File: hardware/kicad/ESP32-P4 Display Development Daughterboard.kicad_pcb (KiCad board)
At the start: 2 copper layers, 130 x 100 mm, 199 parts, among them J1001 SSQ-113-01-G-D, J1002 SSQ-113-01-G-D, J1003 DEBUG HEADER, J201 VEHICLE 12V, J501 SERVICE LINK 5V, J701 NANO DSI 15P, J702 DISPLAYMAN LCD 40P, J801 GT9271 TOUCH 8P, J901 BL HARD DISABLE, Q201 CSD19531Q5A, Q202 CSD19531Q5A, Q301 CSD19531Q5A, Q302 CSD19531Q5A, Q303 CSD19531Q5A, Q304 CSD19531Q5A, Q801 MMBT3904, U201 LM74800QDRRRQ1, U301 LM5176QPWPRQ1, U501 LM76003RNPR, U502 TPS259470ARPWR, U601 TPS3808G01DBVR, U602 LM3880MF-1AA/NOPB, U603 TLV75518PDBVR, U604 TLV75528PDBVR, U605 TPS22919DCKR, U606 SN74LVC1G07DBVR, U607 SN74LVC1G07DBVR, U608 SN74LVC1G07DBVR, U701 TPD6E05U06RVZR, U801 TLV75533PDBVR, U802 TMUX1574PWR, U803 TPD4E05U06DQAR, U901 TPS922053DYYR, U902 SN74LVC1G11DCKR

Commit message: Major fixes. Needs simplification, component organization and routing
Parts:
- J201: footprint Phase2:Molex_Micro-Fit_3.0_43045-0218_2x01-1MP_P3.00mm_Vertical -> Phase2:CONN_SD-43045-007_02_MOL
- J701: footprint Phase2:Amphenol_SFW15R-2STE1LF -> Phase2:Amphenol_CON15_1X15_DRB_SFW_FCI
- J702: footprint Phase2:Molex_505110-4096 -> Phase2:Molex_CON_5051104096
- J801: value GT9271 TOUCH 8P -> Wurth 8pin Top Contact FPC; footprint Connector_FFC-FPC:Hirose_FH12-8S-0.5SH_1x08-1MP_P0.50mm_Horizontal -> Phase2:Wurth_68710814022
- Q201, Q202, Q301, Q302, Q303, Q304: footprint Package_SON:Texas_DQK -> Phase2:Texas_DQJ0008A_VSONP-8
- U502: footprint Phase2:Texas_RPW0010A_VQFN-HR-10_2x2mm -> Phase2:RPW0010A-MFG
- moved TP504 279.8 mm to (-120.5, -63.0)
- moved TP501 272.7 mm to (-103.0, -63.0)
- moved TP503 263.3 mm to (-108.5, -63.0)
- moved R512 252.3 mm to (-106.9, -34.0), turned to 180 degrees
- moved R510 251.8 mm to (-88.5, -48.5)
- moved C513 251.1 mm to (-118.2, -35.0), turned to 180 degrees
- moved R505 249.3 mm to (-114.2, -35.0), turned to 180 degrees
- moved R507 249.2 mm to (-113.3, -27.5), turned to 180 degrees
- moved TP502 249.2 mm to (-114.5, -63.0)
- moved C510 249.1 mm to (-110.5, -40.5)
- moved R506 248.0 mm to (-111.2, -35.0), turned to 180 degrees
- moved C511 246.7 mm to (-103.0, -40.5)
- moved C501 245.5 mm to (-95.7, -44.7)
- moved C502 245.5 mm to (-93.2, -44.2)
- moved C504 245.5 mm to (-90.2, -43.2)
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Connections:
- J1002 pad 25: unconnected-(J1002-GND-Pad25) -> GND
- J1002 pad 26: unconnected-(J1002-GND-Pad26) -> GND
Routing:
- net CTP_RESET_N_NANO: track 0.00 -> 6.07 mm
- net LCD_PWR_EN: track 0.00 -> 3.64 mm
- net LCD_RESET_CMD_N: track 0.00 -> 3.44 mm
- net CTP_INT_NANO: track 0.00 -> 2.89 mm
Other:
- board size 130 x 100 mm -> 150 x 64.6 mm
- board text removed: "Technical drawings derived from Waveshare ESP32-P4-NANO manufacturer DXF; edited/rescaled for KiCad import. Verify against original vendor PDF/DXF/STEP before mechanical freeze."

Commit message: design update
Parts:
- removed H101: M3 LEFT TOP SUPPORT, MountingHole:MountingHole_3.2mm_M3
- removed H102: M3 LEFT BOTTOM SUPPORT, MountingHole:MountingHole_3.2mm_M3
- removed J1003: DEBUG HEADER, Connector_PinHeader_2.54mm:PinHeader_2x05_P2.54mm_Vertical
- removed TP1001: LCD_PWR_EN, TestPoint:TestPoint_THTPad_D1.0mm_Drill0.5mm
- removed TP1002: LCD_RESET_CMD_N, TestPoint:TestPoint_THTPad_D1.0mm_Drill0.5mm
- removed TP1003, TP901: BL_PWM, TestPoint:TestPoint_THTPad_D1.0mm_Drill0.5mm
- removed TP1004: CTP_RESET_N_NANO, TestPoint:TestPoint_THTPad_D1.0mm_Drill0.5mm
- removed TP1005: CTP_INT_NANO, TestPoint:TestPoint_THTPad_D1.0mm_Drill0.5mm
- removed TP1006, TP103: GND, TestPoint:TestPoint_THTPad_D1.0mm_Drill0.5mm
- removed TP201: VEH_12V_RAW, TestPoint:TestPoint_THTPad_D1.0mm_Drill0.5mm
- removed TP202: VEH_PROT, TestPoint:TestPoint_THTPad_D1.0mm_Drill0.5mm
- removed TP301: SYS_24V, TestPoint:TestPoint_THTPad_D1.0mm_Drill0.5mm
- removed TP302: SYS24_PGOOD, TestPoint:TestPoint_THTPad_D1.0mm_Drill0.5mm
- removed TP501: SYS_5V_3A, TestPoint:TestPoint_THTPad_D1.0mm_Drill0.5mm
- removed TP502: NANO_5V, TestPoint:TestPoint_THTPad_D1.0mm_Drill0.5mm
- removed TP503: SYS5_PGOOD, TestPoint:TestPoint_THTPad_D1.0mm_Drill0.5mm
- removed TP504: NANO_EFUSE_FLT, TestPoint:TestPoint_THTPad_D1.0mm_Drill0.5mm
- removed TP601: VIN_GOOD, TestPoint:TestPoint_THTPad_D1.0mm_Drill0.5mm
- removed TP602: SEQ_FLAG1, TestPoint:TestPoint_THTPad_D1.0mm_Drill0.5mm
- removed TP603: SEQ_FLAG2, TestPoint:TestPoint_THTPad_D1.0mm_Drill0.5mm
- removed TP604: SEQ_FLAG3, TestPoint:TestPoint_THTPad_D1.0mm_Drill0.5mm
- removed TP605: LCD_IOVCC, TestPoint:TestPoint_THTPad_D1.0mm_Drill0.5mm
- removed TP606: LCD_VCI, TestPoint:TestPoint_THTPad_D1.0mm_Drill0.5mm
- removed TP607: LCD_RESET_N, TestPoint:TestPoint_THTPad_D1.0mm_Drill0.5mm
- removed TP801: TOUCH_3V3, TestPoint:TestPoint_THTPad_D1.0mm_Drill0.5mm
- removed TP802: CTP_SCL, TestPoint:TestPoint_THTPad_D1.0mm_Drill0.5mm
- removed TP803: CTP_SDA, TestPoint:TestPoint_THTPad_D1.0mm_Drill0.5mm
- removed TP804: CTP_INT, TestPoint:TestPoint_THTPad_D1.0mm_Drill0.5mm
- removed TP805: CTP_RESET_N, TestPoint:TestPoint_THTPad_D1.0mm_Drill0.5mm
- removed TP902: BL_DIM, TestPoint:TestPoint_THTPad_D1.0mm_Drill0.5mm
- removed TP903: LED_A, TestPoint:TestPoint_THTPad_D1.0mm_Drill0.5mm
- removed TP904: LED_K, TestPoint:TestPoint_THTPad_D1.0mm_Drill0.5mm
- removed TP905: BL_FAULT_N, TestPoint:TestPoint_THTPad_D1.0mm_Drill0.5mm
- R206: value 10.0k 1% -> 100R 1%
- moved C508 276.3 mm to (163.2, -40.2), turned to 0 degrees
- moved C509 276.1 mm to (163.2, -37.0), turned to 0 degrees
- moved C510 273.8 mm to (163.2, -33.8)
- moved C511 266.4 mm to (163.2, -30.5)
- moved L501 258.2 mm to (156.7, -36.2), turned to 0 degrees
- moved C501 249.0 mm to (153.0, -31.0), turned to -90 degrees
- moved R504 248.7 mm to (169.5, -22.3)
- moved C502 247.6 mm to (152.9, -16.9)
- moved C504 247.6 mm to (155.9, -15.9)
- moved C513 247.6 mm to (127.9, -7.71)
- moved C514 247.6 mm to (157.6, -5.49)
- moved R501 247.6 mm to (150.9, -12.9)
- moved R502 247.6 mm to (153.9, -12.9)
- moved R503 247.6 mm to (157.4, -16.9)
- moved R505 247.6 mm to (131.9, -7.71)
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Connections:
- C207 pad 2: VEH_PROT -> GND
- U301 pad 13: SYS_24V -> Net-(U301-ISNS+)
- U301 pad 14: SYS_24V -> Net-(U301-ISNS+)
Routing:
- net SYS_24V: track 0.00 -> 39.6 mm, vias 0 -> 4
- net VEH_PROT: track 0.00 -> 32.8 mm, vias 0 -> 15
- net BUCK_SHUNT_HI: track 0.00 -> 19.4 mm, vias 0 -> 2
- net GND: track 0.00 -> 17.2 mm, vias 0 -> 34
- net SW2: track 0.00 -> 16.2 mm
- net VEH_HGATE: track 0.00 -> 15.8 mm
- net SYS_5V_3A: track 0.00 -> 15.5 mm, vias 0 -> 3
- net LDRV2: track 0.00 -> 14.4 mm, vias 0 -> 2
- net HDRV2: track 0.00 -> 14.4 mm, vias 0 -> 2
- net VEH_FILTER: track 0.00 -> 13.9 mm
- net SW1: track 0.00 -> 13.2 mm, vias 0 -> 2
- net HDRV1: track 0.00 -> 10.4 mm, vias 0 -> 2
- net VEH_FET_MID: track 0.00 -> 10.2 mm, vias 0 -> 2
- net SYS24_PGOOD: track 0.00 -> 8.65 mm, vias 0 -> 2
- net LDRV1: track 0.00 -> 7.26 mm, vias 0 -> 2
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- added copper zone on F.Cu, net BUCK_SHUNT_HI
- added copper zone on F.Cu, net SW1
- added copper zone on F.Cu, net SW2
- added copper zone on F.Cu, net SYS_24V
- added copper zone on F.Cu, net VEH_12V_RAW
- added copper zone on F.Cu, net VEH_FET_MID
- added copper zone on F.Cu, net VEH_FILTER
- added copper zone on F.Cu, net VEH_FUSED
- added copper zone on F.Cu, net VEH_PROT
- added copper zone on In2.Cu, net VEH_PROT
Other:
- outline, holes or cut-outs redrawn
- copper layers 2 -> 4

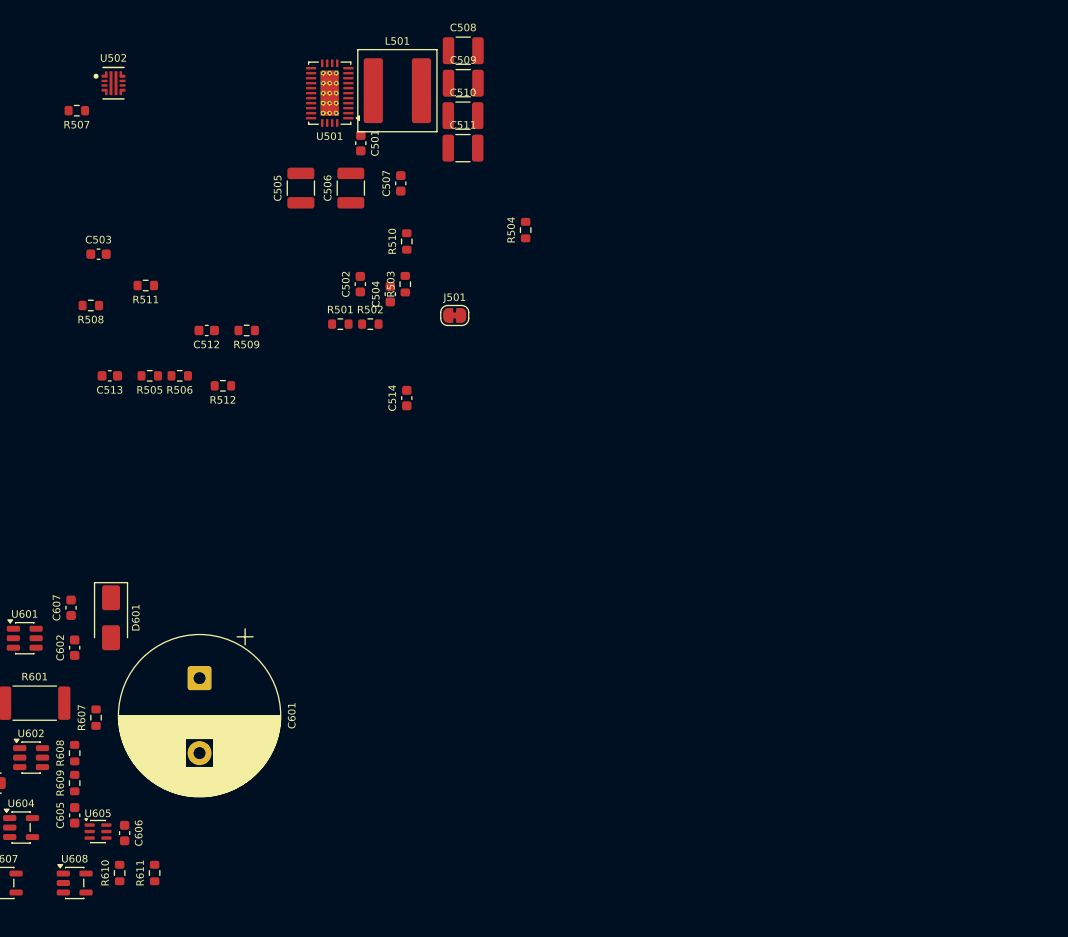
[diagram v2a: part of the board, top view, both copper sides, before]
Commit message: v0.5-nano-baseline (nano-final)
This is the final baseline version of the project to use the Waveshare ESP32-P4-Nano host board. The project will be transitioning to the Waveshare ESP32-P4-WIFI6-DB host board going forward, and no will no longer use the Nano.
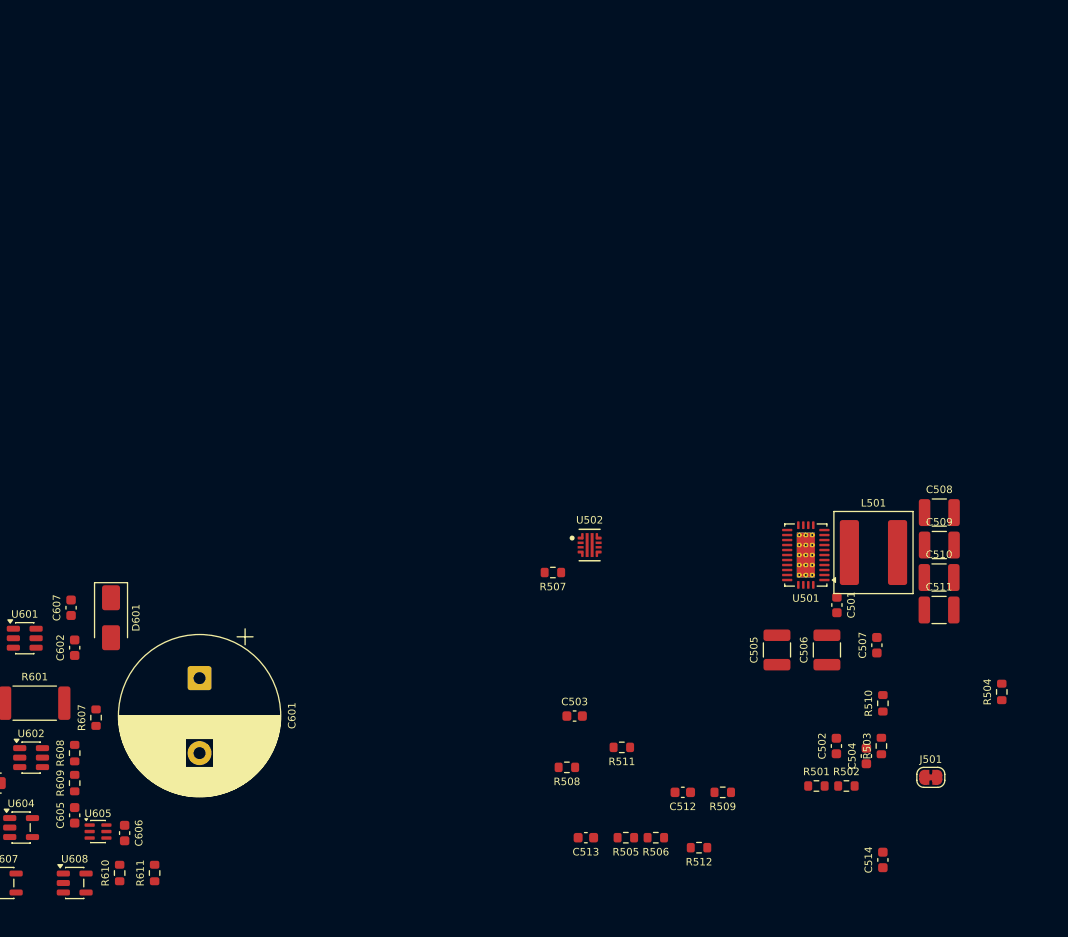
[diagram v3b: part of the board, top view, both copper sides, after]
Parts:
- moved C501 66.4 mm to (200.7, 15.2)
- moved C502 66.4 mm to (200.6, 29.3)
- moved C503 66.4 mm to (174.4, 26.3)
- moved C504 66.4 mm to (203.6, 30.3)
- moved C505 66.4 mm to (194.7, 19.7)
- moved C506 66.4 mm to (199.7, 19.7)
- moved C507 66.4 mm to (204.7, 19.2)
- moved C508 66.4 mm to (210.9, 5.97)
- moved C509 66.4 mm to (210.9, 9.22)
- moved C510 66.4 mm to (210.9, 12.5)
- moved C511 66.4 mm to (210.9, 15.7)
- moved C512 66.4 mm to (185.2, 34.0)
- moved C513 66.4 mm to (175.5, 38.5)
- moved C514 66.4 mm to (205.2, 40.7)
- moved J501 66.4 mm to (210.1, 32.5)
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
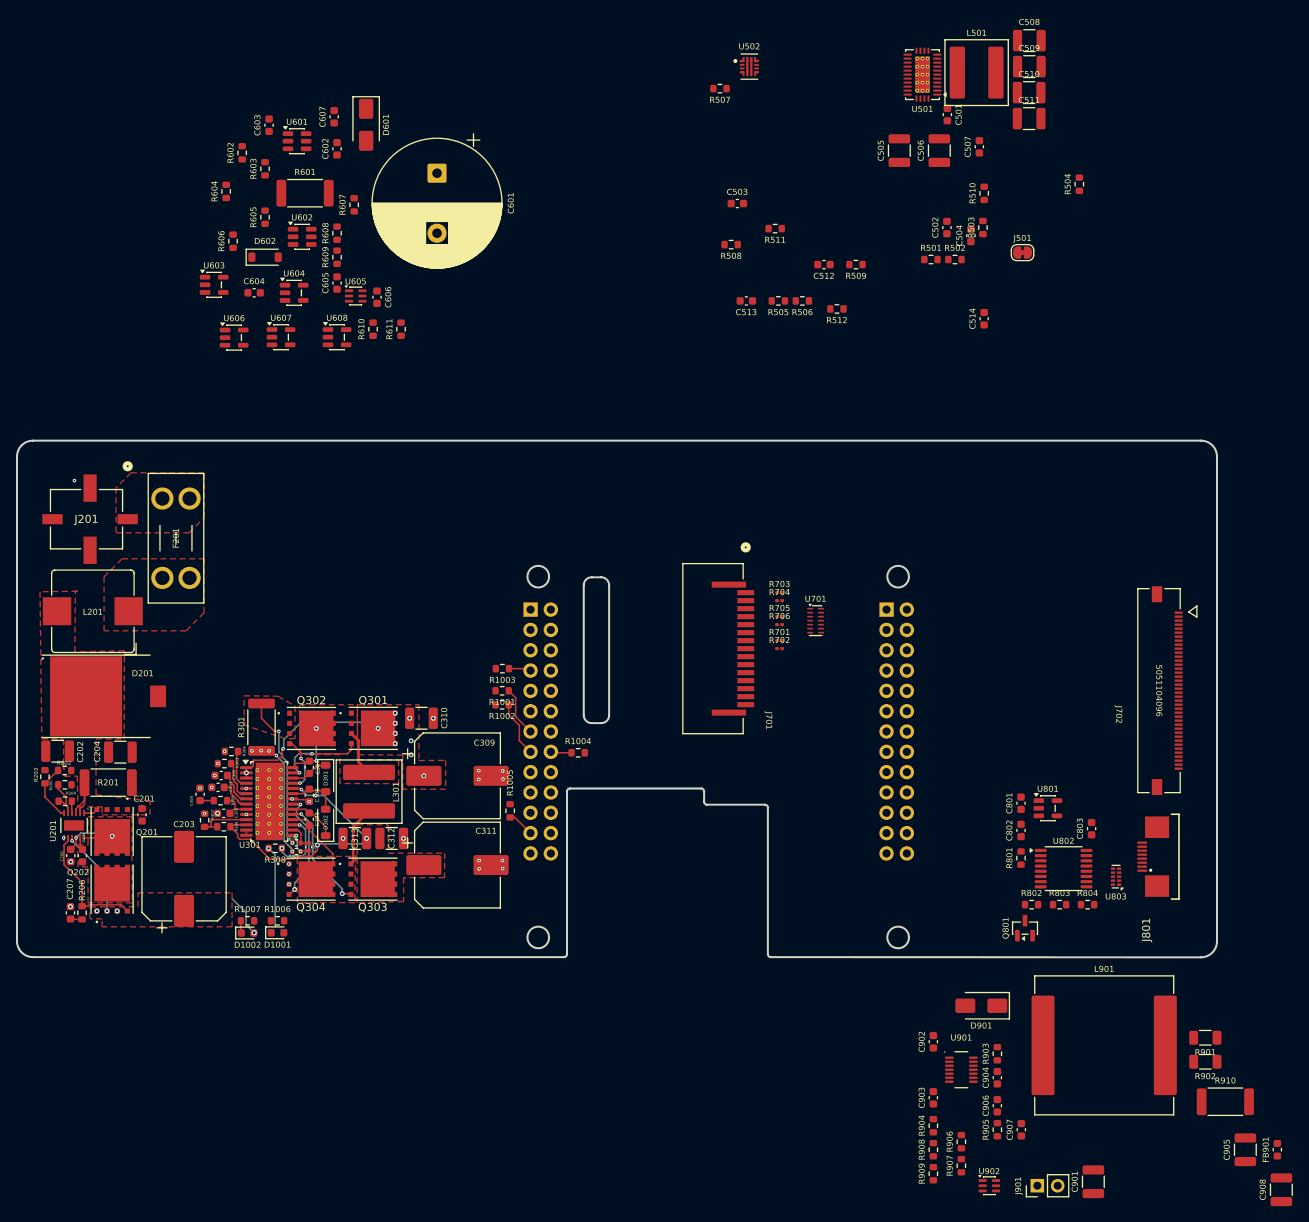
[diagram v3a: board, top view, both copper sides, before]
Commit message: create new firmware for waveshare 8.8" display with touch
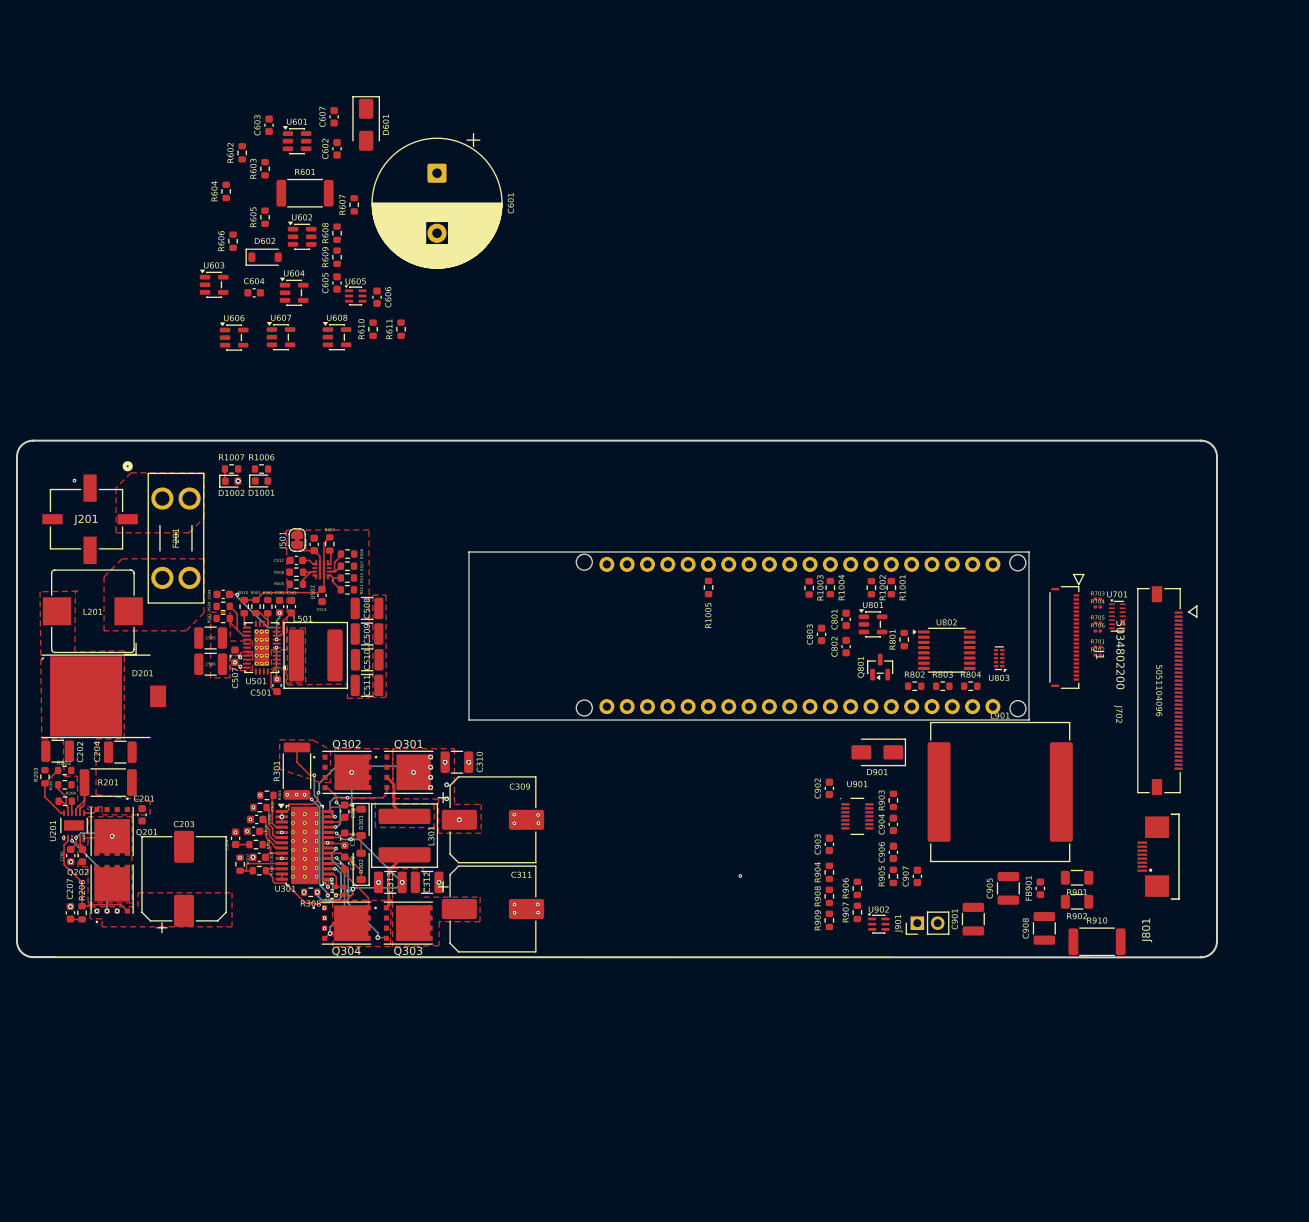
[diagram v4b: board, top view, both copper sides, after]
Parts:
- removed J1001, J1002: SSQ-113-01-G-D, Phase2:Samtec_SSQ-113-01-G-D_BottomMount
- removed J701: NANO DSI 15P, Phase2:Amphenol_CON15_1X15_DRB_SFW_FCI
- added J1: 5034802200, Phase2:CON_5034802200_MOL, F.Cu at (215.3, 80.6)
- added J101: ESP32-P4-WIFI6-DB-P1, PCM_SF-Connector:1x20, F.Cu at (206.3, 71.4)
- added J102: ESP32-P4-WIFI6-DB-P2, PCM_SF-Connector:1x20, F.Cu at (206.3, 89.2)
- C207: value 82nF 25V X7R -> 82nF 100V X7R
- U502: footprint Phase2:RPW0010A-MFG -> Phase2:Texas_RPW0010A_VQFN-HR-10_2x2mm
- moved R504 119.3 mm to (110.1, 76.7), turned to 180 degrees
- moved C507 112.8 mm to (111.6, 82.9), turned to -90 degrees
- moved C506 111.4 mm to (108.6, 83.9), turned to 180 degrees
- moved L501 110.1 mm to (121.7, 82.8)
- moved C501 110.1 mm to (116.9, 86.6)
- moved U501 109.3 mm to (115.0, 81.9)
- moved C508 109.0 mm to (128.1, 77.0)
- moved C509 109.0 mm to (128.1, 80.2)
- moved C510 109.0 mm to (128.1, 83.4)
- moved C511 108.9 mm to (128.1, 86.6)
- moved R503 106.8 mm to (110.1, 78.2), turned to 0 degrees
- moved R510 105.9 mm to (112.8, 76.7)
- moved C505 105.5 mm to (108.6, 80.7), turned to 180 degrees
- moved C504 103.7 mm to (110.1, 75.2), turned to 180 degrees
- moved J501 97.5 mm to (119.4, 68.4), turned to 90 degrees
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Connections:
- net CTP_INT_NANO renamed CTP_INT_HOST
- net CTP_RESET_N_NANO renamed CTP_RESET_N_HOST
- net NANO_3V3_DETECT renamed HOST_3V3_DETECT
- net NANO_5V_EFUSED renamed HOST_5V_EFUSED
- net NANO_EFUSE_FLT renamed HOST_EFUSE_FLT
- J501 pad 2: NANO_5V -> HOST_5V
- R801 pad 1: NANO_3V3_REF -> HOST_3V3_REF
- U802 pad 4: NANO_I2C_SCL -> HOST_I2C_SCL
- U802 pad 7: NANO_I2C_SDA -> HOST_I2C_SDA
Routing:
- net LM760_SS: track 0.00 -> 7.32 mm, vias 0 -> 2
- net LCD_RESET_CMD_N: track 7.01 -> 0.00 mm
- net LM760_EN: track 0.00 -> 6.59 mm
- net LCD_PWR_EN: track 6.22 -> 0.00 mm
- net SYS_5V_3A: track 15.5 -> 21.0 mm
- net HOST_5V_EFUSED: track 0.00 -> 5.10 mm
- net EFUSE_OV: track 0.00 -> 4.34 mm
- net LM760_BOOT: track 0.00 -> 3.98 mm, vias 0 -> 2
- net LM760_SW: track 0.00 -> 3.72 mm
- net LM760_FB: track 0.00 -> 3.56 mm
- net LM760_VCC: track 0.00 -> 3.50 mm, vias 0 -> 2
- net EFUSE_ILM: track 0.00 -> 3.40 mm
- net CTP_INT_HOST: track 3.36 -> 0.00 mm
- net EFUSE_EN: track 0.00 -> 3.26 mm
- net BL_PWM: track 2.79 -> 0.00 mm
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- added copper zone on F.Cu, net GND
- added copper zone on F.Cu, net LM760_SW
- added copper zone on F.Cu, net SYS_5V_3A
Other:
- outline, holes or cut-outs redrawn
